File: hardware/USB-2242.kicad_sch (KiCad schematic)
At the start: 19 parts, among them J1 Bus_M.2_Socket_B, U1 TPS613222ADBV

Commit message: Update project name to respect trademarks
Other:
- title: Logitech Unifying 2242 -> USB 2242
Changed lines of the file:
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@@
 	(paper "USLetter")
 	(title_block
-		(title "Logitech Unifying 2242")
+		(title "USB 2242")
 		(date "2023-03-04")
 		(rev "B")
@@
 		)
 		(instances
-			(project "Logitech Unifying 2242"
+			(project "USB 2242"
 				(path "/1bbba678-0bcb-4cc7-a74d-51164c36ba99"
 					(reference "C1.2")
@@
 		)
 		(instances
-			(project "Logitech Unifying 2242"
+			(project "USB 2242"
 				(path "/1bbba678-0bcb-4cc7-a74d-51164c36ba99"
 					(reference "TP3")
@@
 		)
 		(instances
-			(project "Logitech Unifying 2242"
+			(project "USB 2242"
 				(path "/1bbba678-0bcb-4cc7-a74d-51164c36ba99"
 					(reference "TP1")
@@
 		)
 		(instances
-			(project "Logitech Unifying 2242"
+			(project "USB 2242"
 				(path "/1bbba678-0bcb-4cc7-a74d-51164c36ba99"
 					(reference "#PWR0108")
@@
 		)
 		(instances
-			(project "Logitech Unifying 2242"
+			(project "USB 2242"
 				(path "/1bbba678-0bcb-4cc7-a74d-51164c36ba99"
 					(reference "C3.1")
@@
 		)
 		(instances
-			(project "Logitech Unifying 2242"
+			(project "USB 2242"
 				(path "/1bbba678-0bcb-4cc7-a74d-51164c36ba99"
 					(reference "D1")
@@
 		)
 		(instances
-			(project "Logitech Unifying 2242"
+			(project "USB 2242"
 				(path "/1bbba678-0bcb-4cc7-a74d-51164c36ba99"
 					(reference "#PWR0102")
@@
 		)
 		(instances
-			(project "Logitech Unifying 2242"
+			(project "USB 2242"
 				(path "/1bbba678-0bcb-4cc7-a74d-51164c36ba99"
 					(reference "#PWR0106")
@@
 		)
 		(instances
-			(project "Logitech Unifying 2242"
+			(project "USB 2242"
 				(path "/1bbba678-0bcb-4cc7-a74d-51164c36ba99"
 					(reference "TP2")
@@
 		)
 		(instances
-			(project "Logitech Unifying 2242"
+			(project "USB 2242"
 				(path "/1bbba678-0bcb-4cc7-a74d-51164c36ba99"
 					(reference "TP5")
@@
 		)
 		(instances
-			(project "Logitech Unifying 2242"
+			(project "USB 2242"
 				(path "/1bbba678-0bcb-4cc7-a74d-51164c36ba99"
 					(reference "#PWR02")
@@
 		)
 		(instances
-			(project "Logitech Unifying 2242"
+			(project "USB 2242"
 				(path "/1bbba678-0bcb-4cc7-a74d-51164c36ba99"
 					(reference "#PWR01")
@@
 		)
 		(instances
-			(project "Logitech Unifying 2242"
+			(project "USB 2242"
 				(path "/1bbba678-0bcb-4cc7-a74d-51164c36ba99"
 					(reference "C2")
@@
 		)
 		(instances
-			(project "Logitech Unifying 2242"
+			(project "USB 2242"
 				(path "/1bbba678-0bcb-4cc7-a74d-51164c36ba99"
 					(reference "J1")
@@
 		)
 		(instances
-			(project "Logitech Unifying 2242"
+			(project "USB 2242"
 				(path "/1bbba678-0bcb-4cc7-a74d-51164c36ba99"
 					(reference "#PWR0105")
@@
 		)
 		(instances
-			(project "Logitech Unifying 2242"
+			(project "USB 2242"
 				(path "/1bbba678-0bcb-4cc7-a74d-51164c36ba99"
 					(reference "C3.3")
@@
 		)
 		(instances
-			(project "Logitech Unifying 2242"
+			(project "USB 2242"
 				(path "/1bbba678-0bcb-4cc7-a74d-51164c36ba99"
 					(reference "C1.1")
@@
 		)
 		(instances
-			(project "Logitech Unifying 2242"
+			(project "USB 2242"
 				(path "/1bbba678-0bcb-4cc7-a74d-51164c36ba99"
 					(reference "C1.3")
@@
 		)
 		(instances
-			(project "Logitech Unifying 2242"
+			(project "USB 2242"
 				(path "/1bbba678-0bcb-4cc7-a74d-51164c36ba99"
 					(reference "#PWR0103")
@@
 		)
 		(instances
-			(project "Logitech Unifying 2242"
+			(project "USB 2242"
 				(path "/1bbba678-0bcb-4cc7-a74d-51164c36ba99"
 					(reference "#PWR0107")
@@
 		)
 		(instances
-			(project "Logitech Unifying 2242"
+			(project "USB 2242"
 				(path "/1bbba678-0bcb-4cc7-a74d-51164c36ba99"
 					(reference "F1")
@@
 		)
 		(instances
-			(project "Logitech Unifying 2242"
+			(project "USB 2242"
 				(path "/1bbba678-0bcb-4cc7-a74d-51164c36ba99"
 					(reference "USB1")
@@
 		)
 		(instances
-			(project "Logitech Unifying 2242"
+			(project "USB 2242"
 				(path "/1bbba678-0bcb-4cc7-a74d-51164c36ba99"
 					(reference "C3.2")
@@
 		)
 		(instances
-			(project "Logitech Unifying 2242"
+			(project "USB 2242"
 				(path "/1bbba678-0bcb-4cc7-a74d-51164c36ba99"
 					(reference "R1")
@@
 		)
 		(instances
-			(project "Logitech Unifying 2242"
+			(project "USB 2242"
 				(path "/1bbba678-0bcb-4cc7-a74d-51164c36ba99"
 					(reference "#PWR0109")
@@
 		)
 		(instances
-			(project "Logitech Unifying 2242"
+			(project "USB 2242"
 				(path "/1bbba678-0bcb-4cc7-a74d-51164c36ba99"
 					(reference "#PWR0104")
@@
 		)
 		(instances
-			(project "Logitech Unifying 2242"
+			(project "USB 2242"
 				(path "/1bbba678-0bcb-4cc7-a74d-51164c36ba99"
 					(reference "L1")
@@
 		)
 		(instances
-			(project "Logitech Unifying 2242"
+			(project "USB 2242"
 				(path "/1bbba678-0bcb-4cc7-a74d-51164c36ba99"
 					(reference "U1")
@@
 		)
 		(instances
-			(project "Logitech Unifying 2242"
+			(project "USB 2242"
 				(path "/1bbba678-0bcb-4cc7-a74d-51164c36ba99"
 					(reference "TP4")

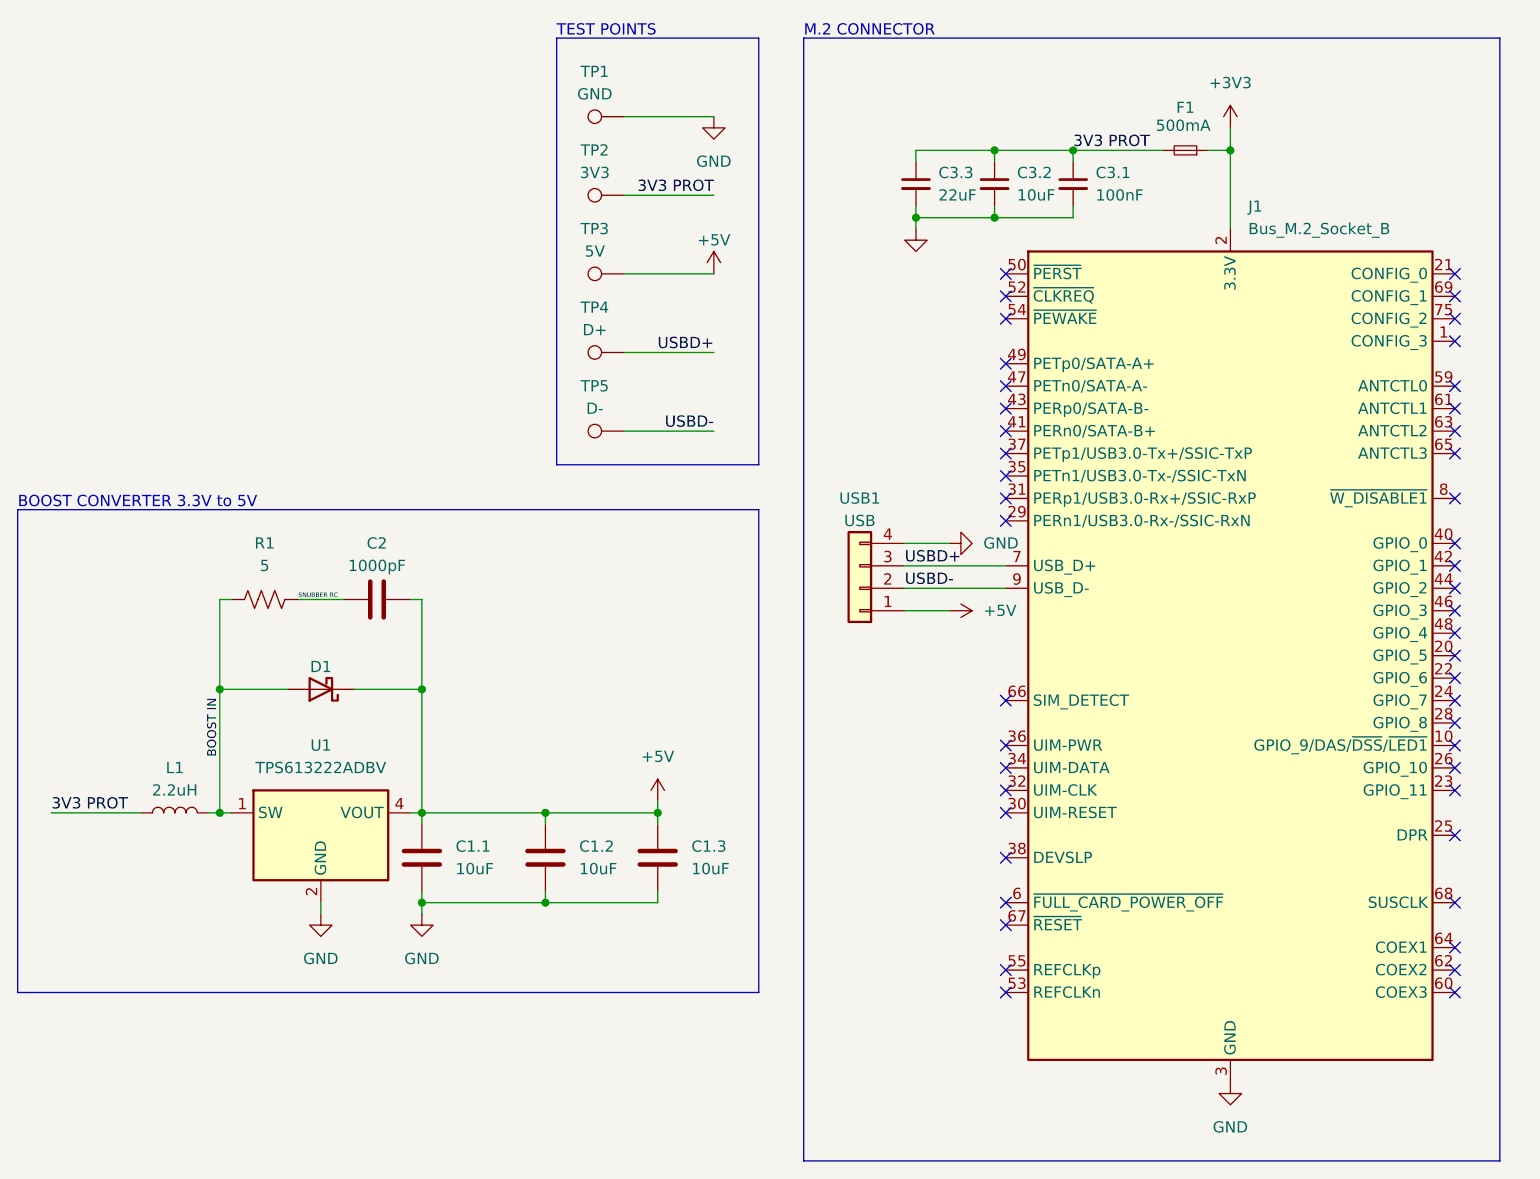
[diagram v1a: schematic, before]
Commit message: Replace USB port and make various minor changes to project
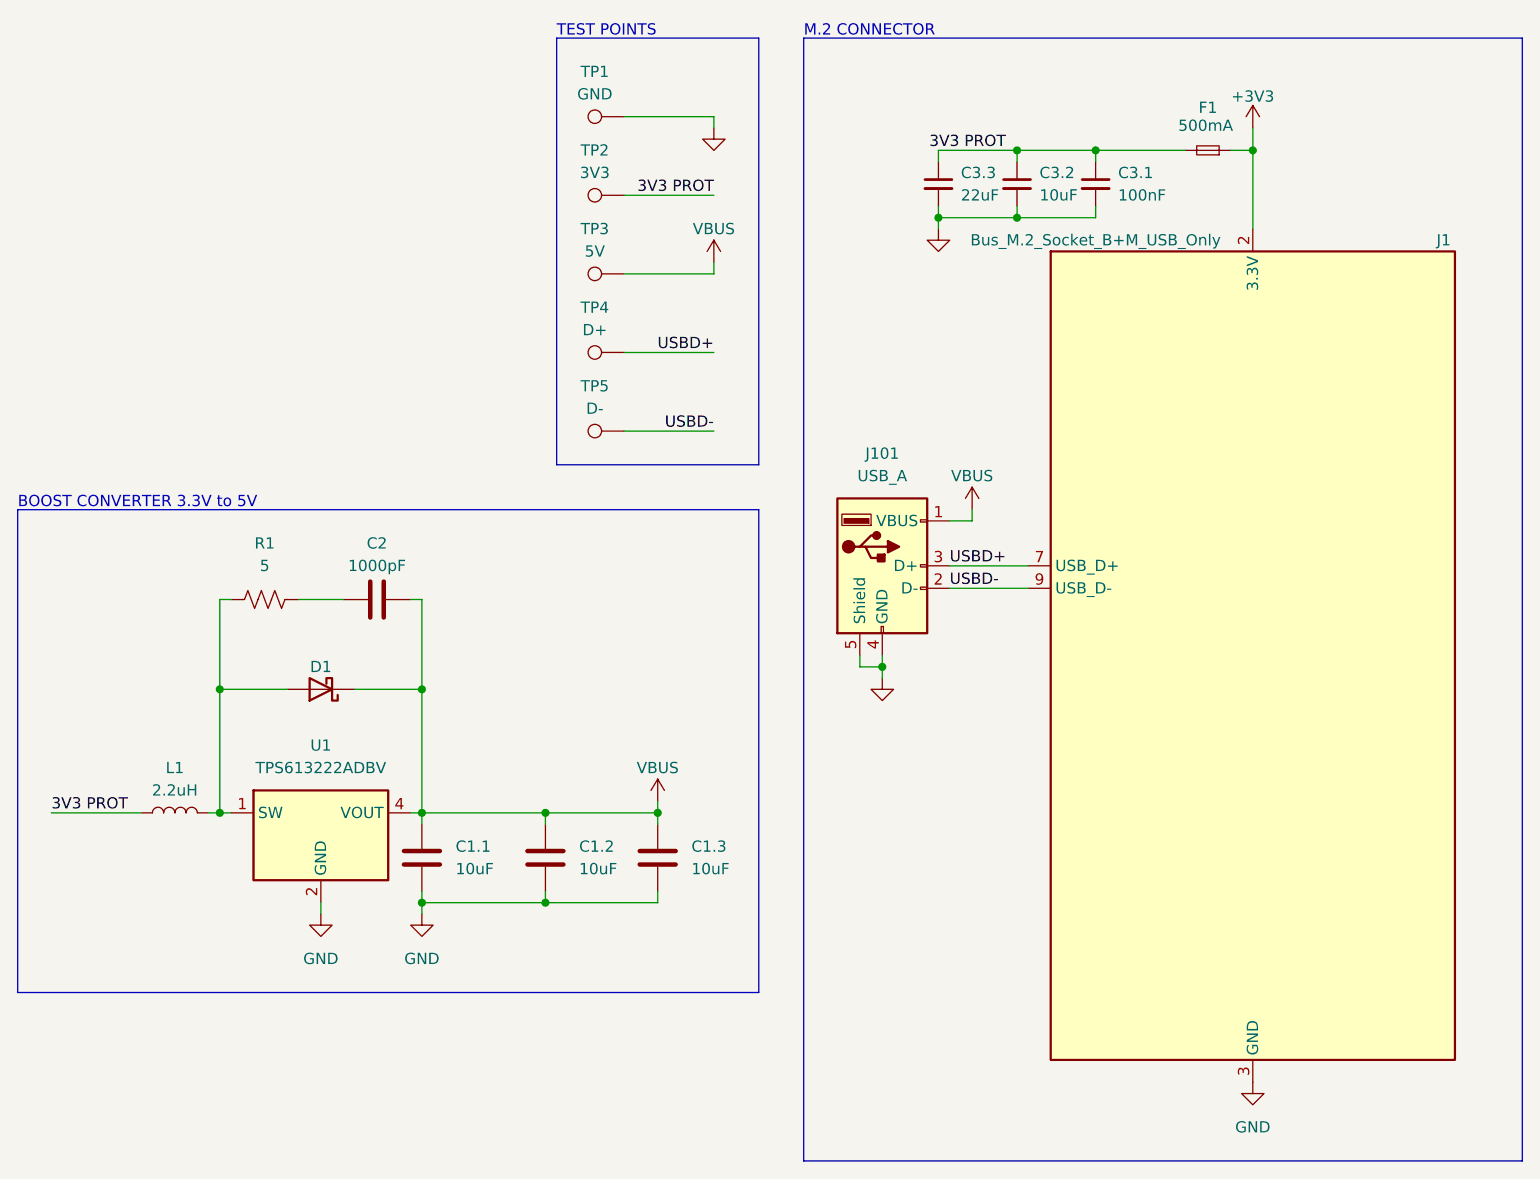
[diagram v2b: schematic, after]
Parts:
- removed USB1: USB, Connector_USB:USB_A_TE_292303-7_Horizontal, symbol Connector_Generic:Conn_01x04
- added J101: USB_A, Adam-Tech:USB-A-S-RA-TSMT, symbol Connector:USB_A
- J1: value Bus_M.2_Socket_B -> Bus_M.2_Socket_B+M_USB_Only; symbol Connector:Bus_M.2_Socket_B -> Generic_Custom:Bus_M.2_Socket_B+M_USB_Only
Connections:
- net GND: now also J101.4 (GND), J101.5 (Shield)
- net USBD+: now also J101.3 (D+)
- net USBD-: now also J101.2 (D-)
- net +5V renamed VBUS
- net VBUS: now also J101.1 (VBUS)
- net BOOST IN: no longer names the net of D1.2 (A), L1.2, R1.1, U1.1 (SW)
- net SNUBBER RC: no longer names the net of C2.1, R1.2
- no-connect marks 47 -> 0
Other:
- company: Ben Owen -> Embedded Shark, LLC
- moved on the sheet: C3.1, C3.2, C3.3, F1
